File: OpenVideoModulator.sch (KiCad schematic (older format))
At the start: 25 parts, among them J1 CONN_6, J2 COMPVIDEO_OUT, J3 SVIDEO_OUT, U1 AD724, Y1 4.433619M

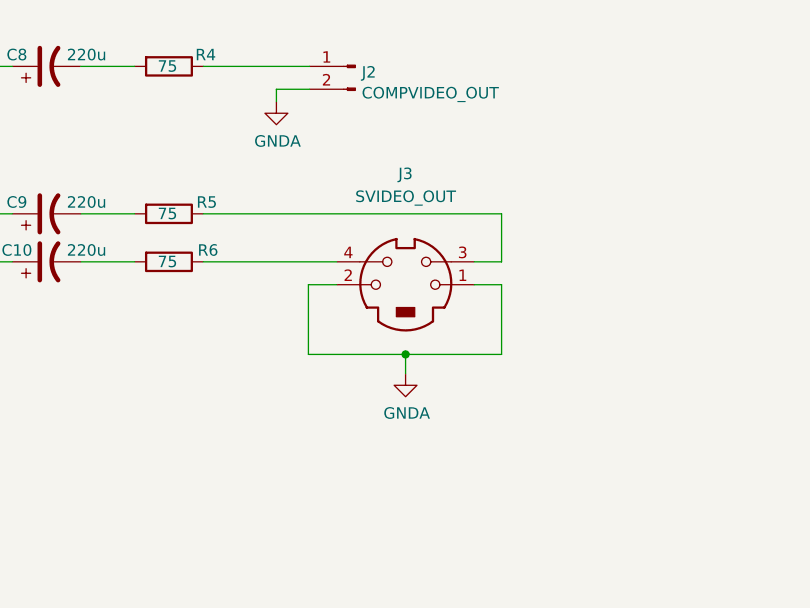
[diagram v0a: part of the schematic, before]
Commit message: Connect MiniDIN shield
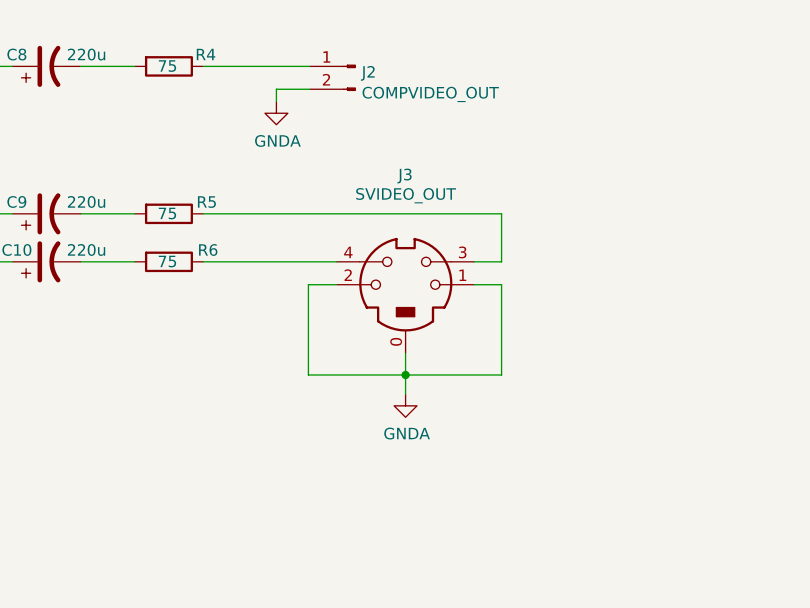
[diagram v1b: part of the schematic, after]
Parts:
- removed J3: SVIDEO_OUT, OpenVideoModulator:MiniDIN4, symbol Connector:Mini-DIN-4
- added J3: SVIDEO_OUT, OpenVideoModulator:MiniDIN4, symbol MiniDIN4WithShield:Mini-DIN-4
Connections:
- net GND: now also J3.0, J3.1, J3.2
- net at R5.1: now also J3.3
- net at R6.1: now also J3.4
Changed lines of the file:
@@
 L power:GNDA #PWR013
 U 1 1 5C9614D8
-P 9365 4780
-F 0 "#PWR013" H 9365 4530 50  0001 C CNN
-F 1 "GNDA" H 9370 4607 50  0000 C CNN
-F 2 "" H 9365 4780 50  0001 C CNN
-F 3 "" H 9365 4780 50  0001 C CNN
-	1    9365 4780
+P 9365 4870
+F 0 "#PWR013" H 9365 4620 50  0001 C CNN
+F 1 "GNDA" H 9370 4697 50  0000 C CNN
+F 2 "" H 9365 4870 50  0001 C CNN
+F 3 "" H 9365 4870 50  0001 C CNN
+	1    9365 4870
 	1    0    0    -1
 $EndComp
 Wire Wire Line
-	9365 4695 9365 4780
+	9365 4785 9365 4870
 Text Label 7025 3435 0    50   ~ 0
 composite
@@
 $EndComp
 $Comp
-L Connector:Mini-DIN-4 J3
-U 1 1 5E91202A
-P 9365 4390
-F 0 "J3" H 9365 4875 50  0000 C CNN
-F 1 "SVIDEO_OUT" H 9365 4775 50  0000 C CNN
-F 2 "OpenVideoModulator:MiniDIN4" H 9365 4390 50  0001 C CNN
-F 3 "http://service.powerdynamics.com/ec/Catalog17/Section%2011.pdf" H 9365 4390 50  0001 C CNN
-	1    9365 4390
-	1    0    0    -1
-$EndComp
-$Comp
 L Connector:Conn_01x02_Male J2
 U 1 1 5E917D59
@@
 	9065 4390 8940 4390
 Wire Wire Line
-	8940 4390 8940 4695
+	8940 4390 8940 4785
 Wire Wire Line
-	8940 4695 9365 4695
+	8940 4785 9365 4785
 Wire Wire Line
-	9785 4695 9785 4390
+	9785 4785 9785 4390
 Wire Wire Line
 	9785 4390 9665 4390
-Connection ~ 9365 4695
+Connection ~ 9365 4785
 Wire Wire Line
-	9365 4695 9785 4695
+	9365 4785 9785 4785
+$Comp
+L MiniDIN4WithShield:Mini-DIN-4 J3
+U 1 1 5E87F227
+P 9365 4390
+F 0 "J3" H 9365 4870 50  0000 C CNN
+F 1 "SVIDEO_OUT" H 9365 4785 50  0000 C CNN
+F 2 "OpenVideoModulator:MiniDIN4" H 9365 4390 50  0001 C CNN
+F 3 "http://service.powerdynamics.com/ec/Catalog17/Section%2011.pdf" H 9365 4390 50  0001 C CNN
+	1    9365 4390
+	1    0    0    -1
+$EndComp
+Wire Wire Line
+	9365 4690 9365 4785
 $EndSCHEMATC
